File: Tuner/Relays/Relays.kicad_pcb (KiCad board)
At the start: 2 copper layers, 100 x 100 mm, 69 parts, among them J1 Conn_01x03, J10 Conn_01x02, J11 Conn_01x02, J12 Conn_01x01, J13 Conn_01x01, J14 Conn_01x01, J15 Conn_01x01, J16 Conn_01x02, J17 Conn_02x10_Odd_Even, J18 Conn_01x02, J19 Conn_01x03, J2 Conn_01x03, J3 Conn_01x03, J4 Conn_01x03, J5 Conn_01x03, J6 Conn_01x03, J7 Conn_01x03, J8 Conn_01x02, J9 Conn_01x02

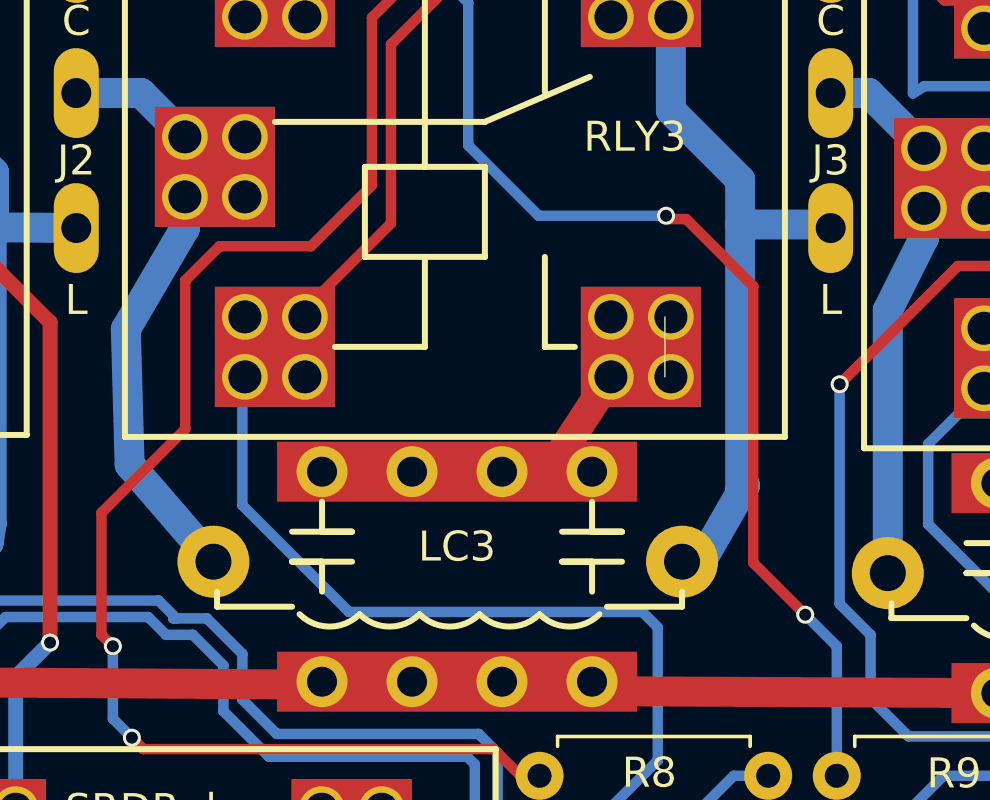
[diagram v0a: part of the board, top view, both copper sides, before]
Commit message: Added RF Shielding to ReversibleSection
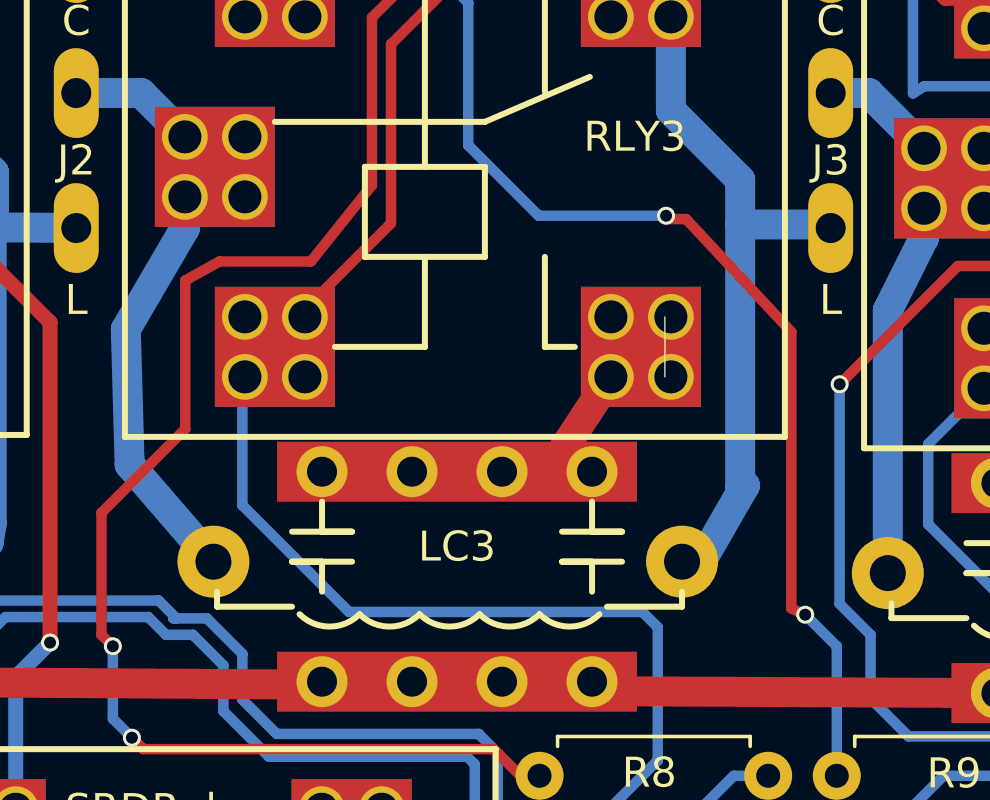
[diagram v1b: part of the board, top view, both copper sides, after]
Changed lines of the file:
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@@
   (segment (start 109.22 106.553) (end 116.586 99.187) (width 0.35) (layer F.Cu) (net 30))
   (segment (start 109.22 112.141) (end 109.22 106.553) (width 0.35) (layer F.Cu) (net 30))
-  (segment (start 107.188 114.173) (end 109.22 112.141) (width 0.35) (layer F.Cu) (net 30))
-  (segment (start 104.14 114.173) (end 107.188 114.173) (width 0.35) (layer F.Cu) (net 30))
-  (segment (start 102.997 115.316) (end 104.14 114.173) (width 0.35) (layer F.Cu) (net 30))
+  (segment (start 107.188 114.681) (end 109.22 112.141) (width 0.35) (layer F.Cu) (net 30))
+  (segment (start 104.14 114.681) (end 107.188 114.681) (width 0.35) (layer F.Cu) (net 30))
+  (segment (start 102.997 115.316) (end 104.14 114.681) (width 0.35) (layer F.Cu) (net 30))
   (segment (start 102.997 120.269) (end 102.997 115.316) (width 0.35) (layer F.Cu) (net 30))
   (segment (start 100.203 123.063) (end 102.997 120.269) (width 0.35) (layer F.Cu) (net 30))
@@
   (segment (start 123.66244 126.45644) (end 124.714 127.508) (width 0.35) (layer B.Cu) (net 31))
   (via (at 123.66244 126.45644) (size 0.6) (drill 0.4) (layers F.Cu B.Cu) (net 31))
-  (segment (start 121.93016 124.72416) (end 123.66244 126.45644) (width 0.35) (layer F.Cu) (net 31))
-  (segment (start 121.93016 115.50396) (end 121.93016 124.72416) (width 0.35) (layer F.Cu) (net 31))
-  (segment (start 119.69496 113.26876) (end 121.93016 115.50396) (width 0.35) (layer F.Cu) (net 31))
+  (segment (start 123.20016 126.24816) (end 123.66244 126.45644) (width 0.35) (layer F.Cu) (net 31))
+  (segment (start 123.20016 117.02796) (end 123.20016 126.24816) (width 0.35) (layer F.Cu) (net 31))
+  (segment (start 119.69496 113.26876) (end 123.20016 117.02796) (width 0.35) (layer F.Cu) (net 31))
   (segment (start 119.13616 113.26876) (end 119.69496 113.26876) (width 0.35) (layer F.Cu) (net 31))
   (segment (start 119.0244 113.157) (end 119.13616 113.26876) (width 0.35) (layer F.Cu) (net 31))

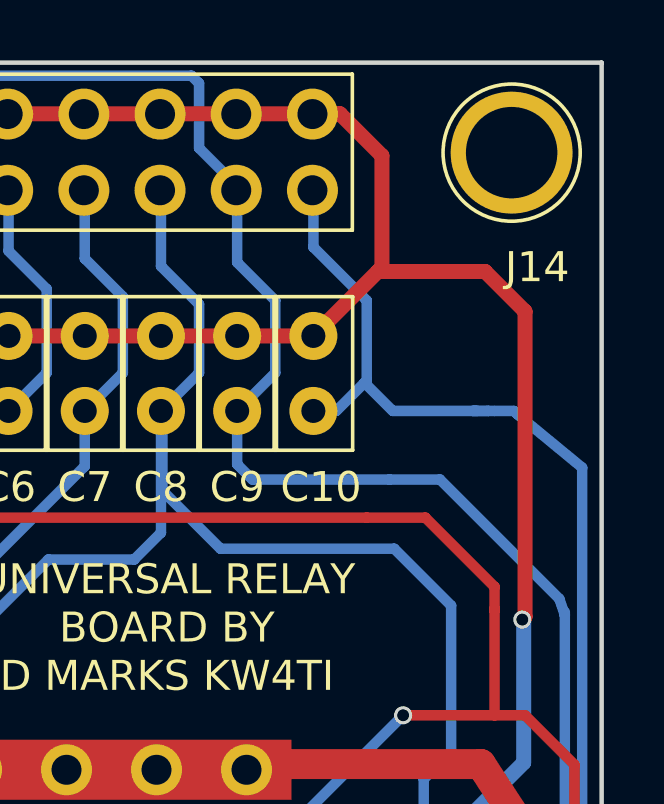
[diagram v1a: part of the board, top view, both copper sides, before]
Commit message: JLCPCB submitted RelayControl version
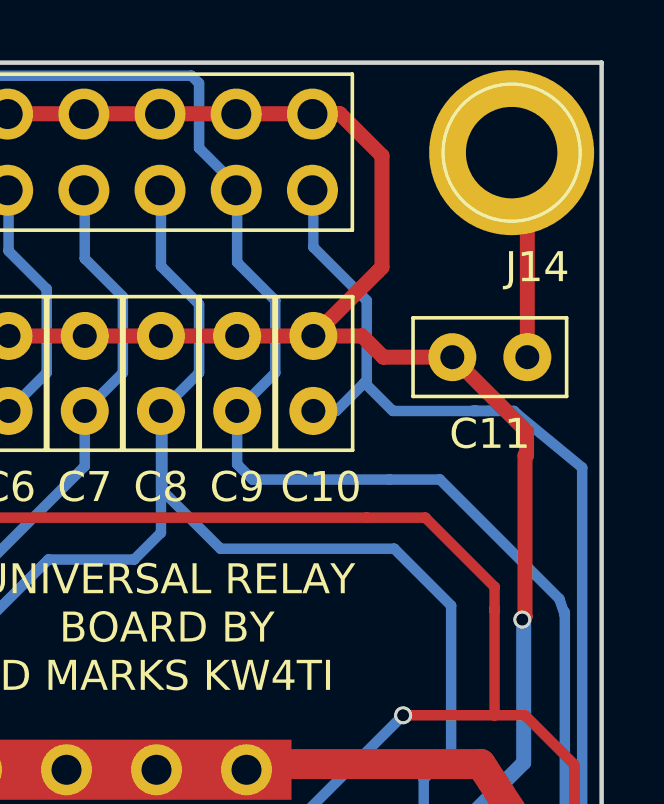
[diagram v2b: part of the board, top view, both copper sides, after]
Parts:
- added C11: 10 nF, Capacitors_THT:C_Disc_D5.0mm_W2.5mm_P2.50mm, F.Cu at (147.5, 59.8)
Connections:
- J14 pad 1: (no net) -> Net-(C11-Pad1)
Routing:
- net Net-(C11-Pad1): track 0.00 -> 7.03 mm
- net +5V: track 424.3 -> 423.3 mm
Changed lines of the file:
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@@
 (kicad_pcb (version 4) (host pcbnew 4.0.7)
   (general
-    (links 517)
+    (links 519)
     (no_connects 0)
     (area 49.924999 49.924999 150.075001 150.075001)
     (thickness 1.6)
     (drawings 14)
-    (tracks 871)
+    (tracks 878)
     (zones 0)
-    (modules 69)
-    (nets 56)
+    (modules 70)
+    (nets 57)
   )
   (page A4)
@@
   )
   (setup
-    (last_trace_width 0.25)
+    (last_trace_width 0.5)
     (user_trace_width 0.35)
     (user_trace_width 0.5)
@@
     (mod_text_size 1 1)
     (mod_text_width 0.15)
-    (pad_size 4.064 4.064)
+    (pad_size 5.5 5.5)
     (pad_drill 3.048)
     (pad_to_mask_clearance 0.2)
@@
   (net 54 "Net-(J19-Pad1)")
   (net 55 "Net-(LC8-Pad1)")
+  (net 56 "Net-(C11-Pad1)")
   (net_class Default "This is the default net class."
     (clearance 0.2)
@@
     (uvia_drill 0.1)
     (add_net +5V)
+    (add_net "Net-(C11-Pad1)")
     (add_net "Net-(D1-Pad1)")
     (add_net "Net-(D10-Pad1)")
@@
     (fp_circle (center 0 0) (end 2.6 0) (layer F.CrtYd) (width 0.05))
     (fp_circle (center 0 0) (end 0 -2.286) (layer F.SilkS) (width 0.12))
-    (pad 1 thru_hole circle (at 0 0) (size 4.064 4.064) (drill 3.048) (layers *.Cu *.Mask))
+    (pad 1 thru_hole circle (at 0 0) (size 5.5 5.5) (drill 3.048) (layers *.Cu *.Mask)
+      (net 56 "Net-(C11-Pad1)"))
   )
   (module Connectors:1pin (layer F.Cu)
@@
     )
   )
+  (module Capacitors_THT:C_Disc_D5.0mm_W2.5mm_P2.50mm (layer F.Cu)
+    (at 147.5232 59.817 180)
+    (descr "C, Disc series, Radial, pin pitch=2.50mm, , diameter*width=5*2.5mm^2, Capacitor, http://cdn-reichelt.de/documents/datenblatt/B300/DS_KERKO_TC.pdf")
+    (tags "C Disc series Radial pin pitch 2.50mm  diameter 5mm width 2.5mm Capacitor")
+    (fp_text reference C11 (at 1.25 -2.56 180) (layer F.SilkS)
+      (effects (font (size 1 1) (thickness 0.15)))
+    )
+    (fp_text value "10 nF" (at 1.25 2.56 180) (layer F.Fab)
+      (effects (font (size 1 1) (thickness 0.15)))
+    )
+    (fp_line (start -1.25 -1.25) (end -1.25 1.25) (layer F.Fab) (width 0.1))
+    (fp_line (start -1.25 1.25) (end 3.75 1.25) (layer F.Fab) (width 0.1))
+    (fp_line (start 3.75 1.25) (end 3.75 -1.25) (layer F.Fab) (width 0.1))
+    (fp_line (start 3.75 -1.25) (end -1.25 -1.25) (layer F.Fab) (width 0.1))
+    (fp_line (start -1.31 -1.31) (end 3.81 -1.31) (layer F.SilkS) (width 0.12))
+    (fp_line (start -1.31 1.31) (end 3.81 1.31) (layer F.SilkS) (width 0.12))
+    (fp_line (start -1.31 -1.31) (end -1.31 1.31) (layer F.SilkS) (width 0.12))
+    (fp_line (start 3.81 -1.31) (end 3.81 1.31) (layer F.SilkS) (width 0.12))
+    (fp_line (start -1.6 -1.6) (end -1.6 1.6) (layer F.CrtYd) (width 0.05))
+    (fp_line (start -1.6 1.6) (end 4.1 1.6) (layer F.CrtYd) (width 0.05))
+    (fp_line (start 4.1 1.6) (end 4.1 -1.6) (layer F.CrtYd) (width 0.05))
+    (fp_line (start 4.1 -1.6) (end -1.6 -1.6) (layer F.CrtYd) (width 0.05))
+    (fp_text user %R (at 1.25 0 180) (layer F.Fab)
+      (effects (font (size 1 1) (thickness 0.15)))
+    )
+    (pad 1 thru_hole circle (at 0 0 180) (size 1.6 1.6) (drill 0.8) (layers *.Cu *.Mask)
+      (net 56 "Net-(C11-Pad1)"))
+    (pad 2 thru_hole circle (at 2.5 0 180) (size 1.6 1.6) (drill 0.8) (layers *.Cu *.Mask)
+      (net 33 +5V))
+    (model ${KISYS3DMOD}/Capacitors_THT.3dshapes/C_Disc_D5.0mm_W2.5mm_P2.50mm.wrl
+      (at (xyz 0 0 0))
+      (scale (xyz 1 1 1))
+      (rotate (xyz 0 0 0))
+    )
+  )
   (gr_text 1 (at 115.316 54.229) (layer F.SilkS)
     (effects (font (size 1 1) (thickness 0.15)))
@@
   (segment (start 135.31088 54.24424) (end 135.31088 56.78424) (width 0.35) (layer B.Cu) (net 32))
   (segment (start 135.31088 56.78424) (end 136.58088 58.05424) (width 0.35) (layer B.Cu) (net 32))
+  (segment (start 147.4978 62.31128) (end 147.4978 62.2916) (width 0.5) (layer F.Cu) (net 33))
+  (segment (start 147.4978 63.08852) (end 147.447 63.08852) (width 0.5) (layer F.Cu) (net 33))
+  (segment (start 147.4978 62.31128) (end 147.4978 63.08852) (width 0.5) (layer F.Cu) (net 33))
+  (segment (start 140.7028 95.04884) (end 139.47648 93.82252) (width 0.5) (layer F.Cu) (net 33))
+  (segment (start 147.447 68.47332) (end 147.447 63.08852) (width 0.5) (layer F.Cu) (net 33))
+  (segment (start 147.35556 68.56476) (end 147.447 68.47332) (width 0.5) (layer F.Cu) (net 33))
+  (via (at 147.35556 68.56476) (size 0.6) (drill 0.4) (layers F.Cu B.Cu) (net 33))
+  (segment (start 147.40128 68.61048) (end 147.35556 68.56476) (width 0.5) (layer B.Cu) (net 33))
+  (segment (start 147.40128 73.33488) (end 147.40128 68.61048) (width 0.5) (layer B.Cu) (net 33))
+  (segment (start 144.82064 75.91552) (end 147.40128 73.33488) (width 0.5) (layer B.Cu) (net 33))
+  (via (at 144.82064 75.91552) (size 0.6) (drill 0.4) (layers F.Cu B.Cu) (net 33))
+  (segment (start 144.82064 86.74608) (end 144.82064 75.91552) (width 0.5) (layer F.Cu) (net 33))
+  (segment (start 143.77924 87.78748) (end 144.82064 86.74608) (width 0.5) (layer F.Cu) (net 33))
+  (segment (start 141.097 87.78748) (end 143.77924 87.78748) (width 0.5) (layer F.Cu) (net 33))
+  (segment (start 139.47648 89.408) (end 141.097 87.78748) (width 0.5) (layer F.Cu) (net 33))
+  (segment (start 139.47648 93.82252) (end 139.47648 89.408) (width 0.5) (layer F.Cu) (net 33))
+  (segment (start 147.4978 62.2916) (end 145.0232 59.817) (width 0.5) (layer F.Cu) (net 33))
+  (segment (start 140.39088 59.11024) (end 142.01584 59.11024) (width 0.5) (layer F.Cu) (net 33))
+  (segment (start 142.01584 59.11024) (end 142.7226 59.817) (width 0.5) (layer F.Cu) (net 33))
+  (segment (start 142.7226 59.817) (end 145.0232 59.817) (width 0.5) (layer F.Cu) (net 33))
   (segment (start 140.39088 51.70424) (end 141.27988 51.70424) (width 0.5) (layer F.Cu) (net 33))
   (segment (start 141.27988 51.70424) (end 142.67688 53.10124) (width 0.5) (layer F.Cu) (net 33))
@@
   (segment (start 97.97034 100.00742) (end 96.50476 101.473) (width 0.5) (layer F.Cu) (net 33))
   (segment (start 140.7028 95.821) (end 140.7028 95.04884) (width 0.5) (layer F.Cu) (net 33))
-  (segment (start 140.7028 95.04884) (end 139.47648 93.82252) (width 0.5) (layer F.Cu) (net 33))
-  (segment (start 139.47648 93.82252) (end 139.47648 89.408) (width 0.5) (layer F.Cu) (net 33))
-  (segment (start 139.47648 89.408) (end 141.097 87.78748) (width 0.5) (layer F.Cu) (net 33))
-  (segment (start 141.097 87.78748) (end 143.77924 87.78748) (width 0.5) (layer F.Cu) (net 33))
-  (segment (start 143.77924 87.78748) (end 144.82064 86.74608) (width 0.5) (layer F.Cu) (net 33))
-  (segment (start 144.82064 86.74608) (end 144.82064 75.91552) (width 0.5) (layer F.Cu) (net 33))
-  (via (at 144.82064 75.91552) (size 0.6) (drill 0.4) (layers F.Cu B.Cu) (net 33))
-  (segment (start 144.82064 75.91552) (end 147.40128 73.33488) (width 0.5) (layer B.Cu) (net 33))
-  (segment (start 147.40128 73.33488) (end 147.40128 68.61048) (width 0.5) (layer B.Cu) (net 33))
-  (segment (start 147.40128 68.61048) (end 147.35556 68.56476) (width 0.5) (layer B.Cu) (net 33))
-  (via (at 147.35556 68.56476) (size 0.6) (drill 0.4) (layers F.Cu B.Cu) (net 33))
-  (segment (start 147.35556 68.56476) (end 147.447 68.47332) (width 0.5) (layer F.Cu) (net 33))
-  (segment (start 147.447 68.47332) (end 147.447 58.293) (width 0.5) (layer F.Cu) (net 33))
-  (segment (start 147.447 58.293) (end 146.11604 56.96204) (width 0.5) (layer F.Cu) (net 33))
-  (segment (start 146.11604 56.96204) (end 142.53908 56.96204) (width 0.5) (layer F.Cu) (net 33))
   (segment (start 88.053799 59.162334) (end 88.773 58.4835) (width 0.5) (layer F.Cu) (net 33))
   (segment (start 91.8205 55.436) (end 94.6221 55.436) (width 0.5) (layer F.Cu) (net 33))
@@
   (segment (start 61.20284 84.0496) (end 64.09308 81.15936) (width 1) (layer F.Cu) (net 55) (status 20))
   (segment (start 64.09308 81.15936) (end 64.09308 80.45984) (width 1) (layer F.Cu) (net 55) (status 30))
+  (segment (start 147.5232 59.817) (end 147.5232 53.5232) (width 0.5) (layer F.Cu) (net 56) (status C00000))
+  (segment (start 147.5232 53.5232) (end 147 53) (width 0.5) (layer F.Cu) (net 56) (status C00000))
 )

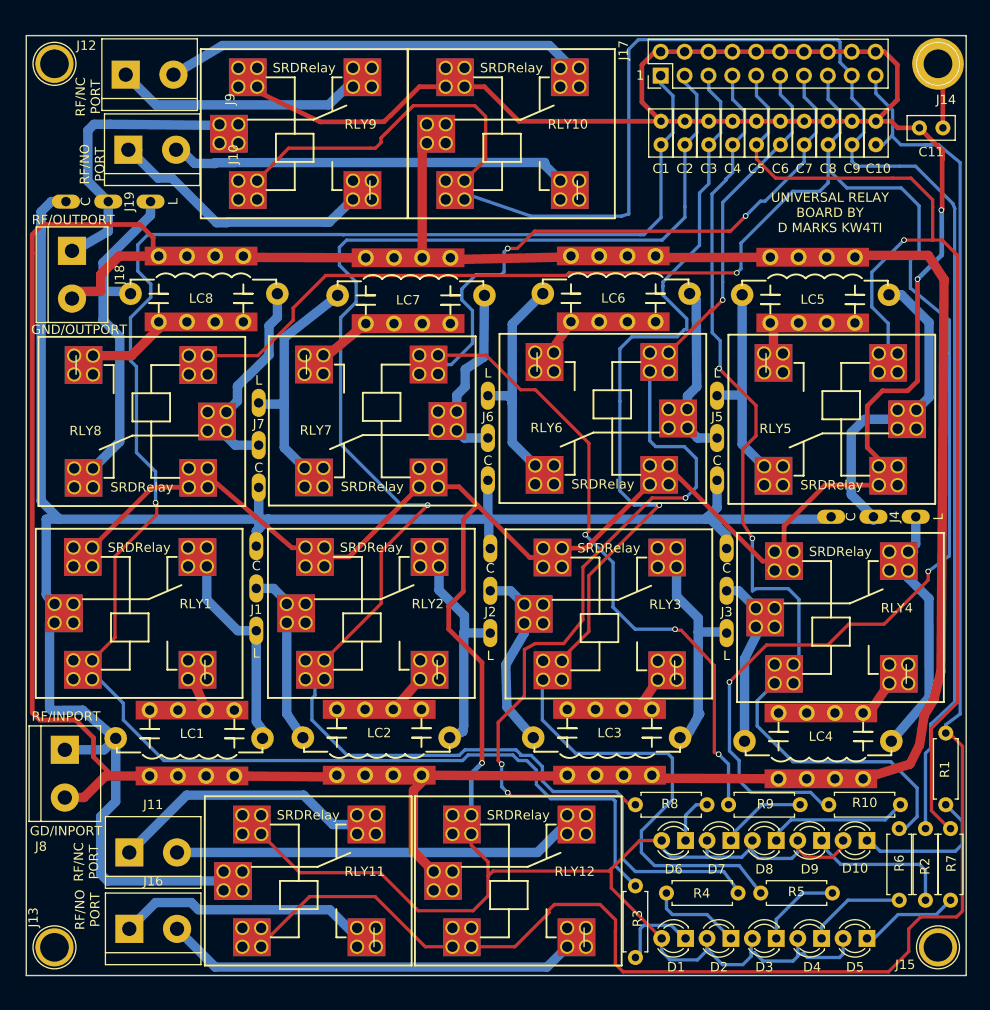
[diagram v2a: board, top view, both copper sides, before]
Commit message: JLCPCB order 09232018 - improved grounding - improved I2C cabling - NEO7M port - support for common mode chokes - relay board now has capacitors on all coils
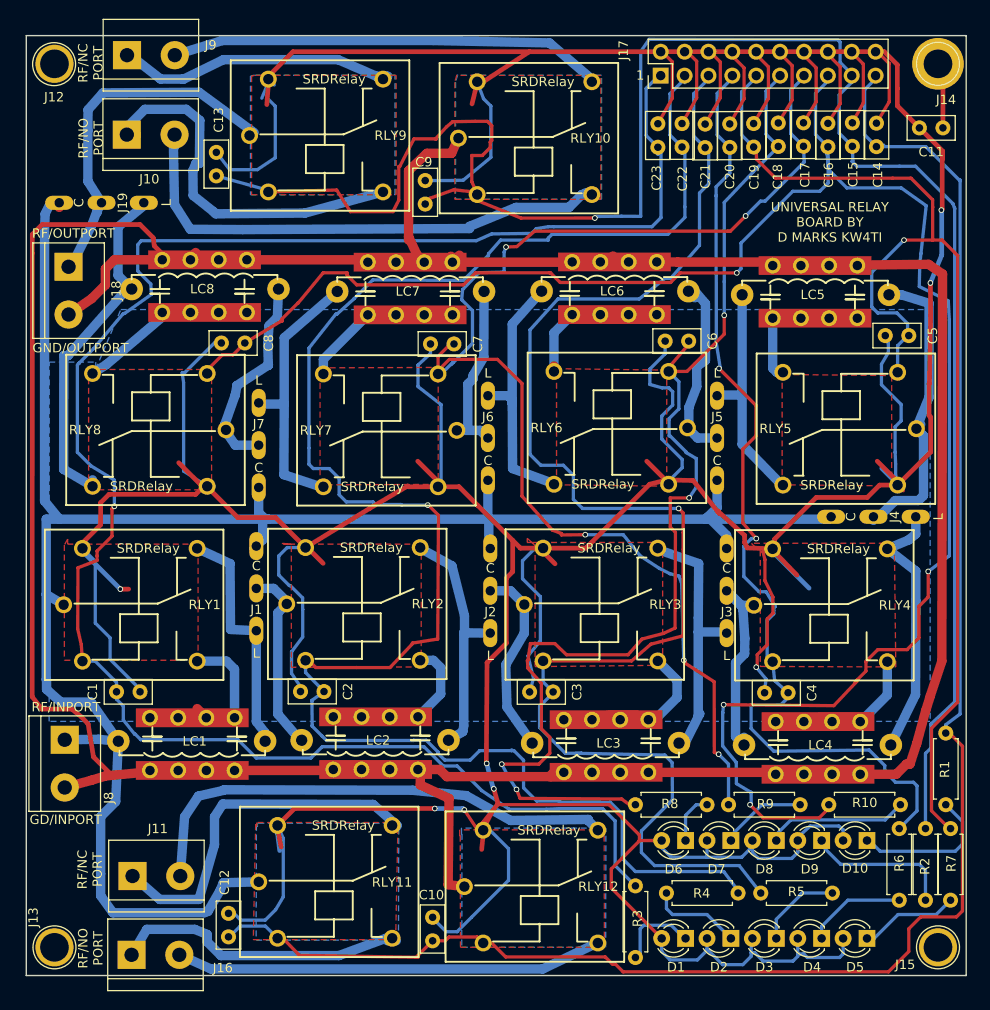
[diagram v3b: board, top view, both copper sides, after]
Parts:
- added C12: 10 nF, Capacitors_THT:C_Disc_D5.0mm_W2.5mm_P2.50mm, F.Cu at (71.5, 145.9)
- added C13: 10 nF, Capacitors_THT:C_Disc_D5.0mm_W2.5mm_P2.50mm, F.Cu at (70.2, 64.9)
- added C14: 10 nF, Capacitors_THT:C_Disc_D5.0mm_W2.5mm_P2.50mm, F.Cu at (140.5, 61.8)
- added C15: 10 nF, Capacitors_THT:C_Disc_D5.0mm_W2.5mm_P2.50mm, F.Cu at (137.9, 61.8)
- added C16: 10 nF, Capacitors_THT:C_Disc_D5.0mm_W2.5mm_P2.50mm, F.Cu at (135.3, 61.8)
- added C17: 10 nF, Capacitors_THT:C_Disc_D5.0mm_W2.5mm_P2.50mm, F.Cu at (132.7, 61.8)
- added C18: 10 nF, Capacitors_THT:C_Disc_D5.0mm_W2.5mm_P2.50mm, F.Cu at (130.0, 61.8)
- added C19: 10 nF, Capacitors_THT:C_Disc_D5.0mm_W2.5mm_P2.50mm, F.Cu at (127.4, 61.9)
- added C20: 10 nF, Capacitors_THT:C_Disc_D5.0mm_W2.5mm_P2.50mm, F.Cu at (124.8, 61.9)
- added C21: 10 nF, Capacitors_THT:C_Disc_D5.0mm_W2.5mm_P2.50mm, F.Cu at (122.2, 61.9)
- added C22: 10 nF, Capacitors_THT:C_Disc_D5.0mm_W2.5mm_P2.50mm, F.Cu at (119.8, 61.9)
- added C23: 10 nF, Capacitors_THT:C_Disc_D5.0mm_W2.5mm_P2.50mm, F.Cu at (117.2, 61.9)
- moved C10 96.9 mm to (93.2, 146.3)
- moved C1 82.1 mm to (59.6, 119.8), turned to 0 degrees
- moved C2 69.7 mm to (81.7, 119.8), turned to 180 degrees
- moved C8 65.5 mm to (73.3, 82.7), turned to 180 degrees
- moved C3 60.5 mm to (106.1, 119.8), turned to 180 degrees
- moved C4 58.6 mm to (131.1, 119.9), turned to 180 degrees
- moved C9 45.8 mm to (92.4, 67.9)
- moved C7 42.9 mm to (95.5, 82.8), turned to 180 degrees
- moved C5 26.0 mm to (143.9, 81.9), turned to 180 degrees
- moved C6 23.1 mm to (120.5, 82.5), turned to 180 degrees
- moved RLY11 3.89 mm to (82.7, 140.0)
- moved RLY10 3.66 mm to (104.0, 60.9)
- moved RLY12 3.64 mm to (104.6, 140.5)
- moved RLY9 3.41 mm to (81.8, 60.6)
- moved J16 2.77 mm to (61.2, 147.8)
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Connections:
- net Net-(LC1-Pad1) renamed BYPASS
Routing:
- net +5V: track 423.3 -> 742.9 mm, vias 3 -> 8
- net RLY3: track 127.3 -> 154.7 mm
- net RLY9: track 190.5 -> 209.4 mm, vias 0 -> 1
- net RLY2: track 173.8 -> 191.3 mm
- net RLY6: track 113.1 -> 128.6 mm
- net Net-(J10-Pad2): track 44.4 -> 57.4 mm
- net Net-(J10-Pad1): track 30.6 -> 41.1 mm
- net RLY8: track 193.1 -> 203.3 mm, vias 3 -> 4
- net RFSIG: track 207.9 -> 218.0 mm
- net Net-(J11-Pad1): track 29.1 -> 38.5 mm
- net Net-(J11-Pad2): track 43.7 -> 52.8 mm
- net RFGND: track 305.8 -> 297.2 mm
- net BYPASS: track 3.88 -> 10.9 mm
- net Net-(J3-Pad2): track 16.3 -> 22.3 mm
- net RLY7: track 133.5 -> 139.0 mm
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- added copper zone on B.Cu, net +5V
- added copper zone on F.Cu, net +5V
